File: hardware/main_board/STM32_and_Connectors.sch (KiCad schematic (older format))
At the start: 26 parts, among them J401 Conn_01x20, J402 Conn_01x20, J403 Conn_01x04, J404 Conn_01x04, J405 Conn_01x04, J406 MOTOR 1, J407 MOTOR 2, J408 POWER, J409 SKITTLE PICKUP, J410 LIMIT SWITCHES, J411 SERVO, Q401 SSM3K333R

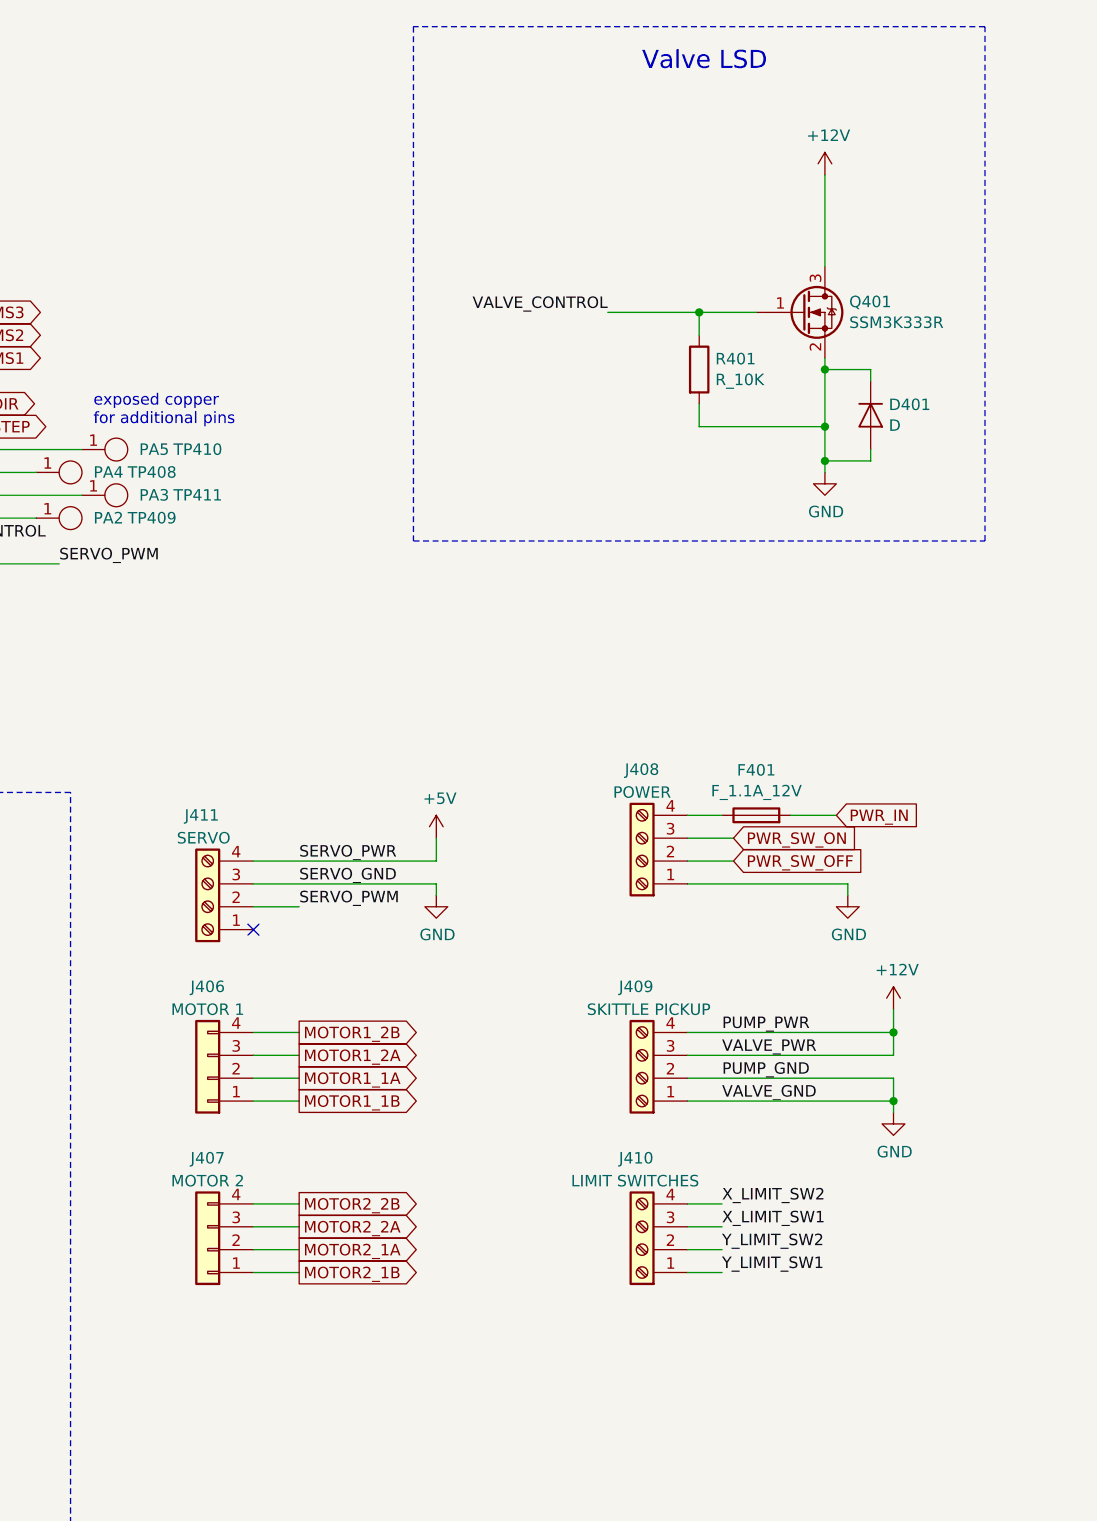
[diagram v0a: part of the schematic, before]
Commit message: fixed valve lsd circuit
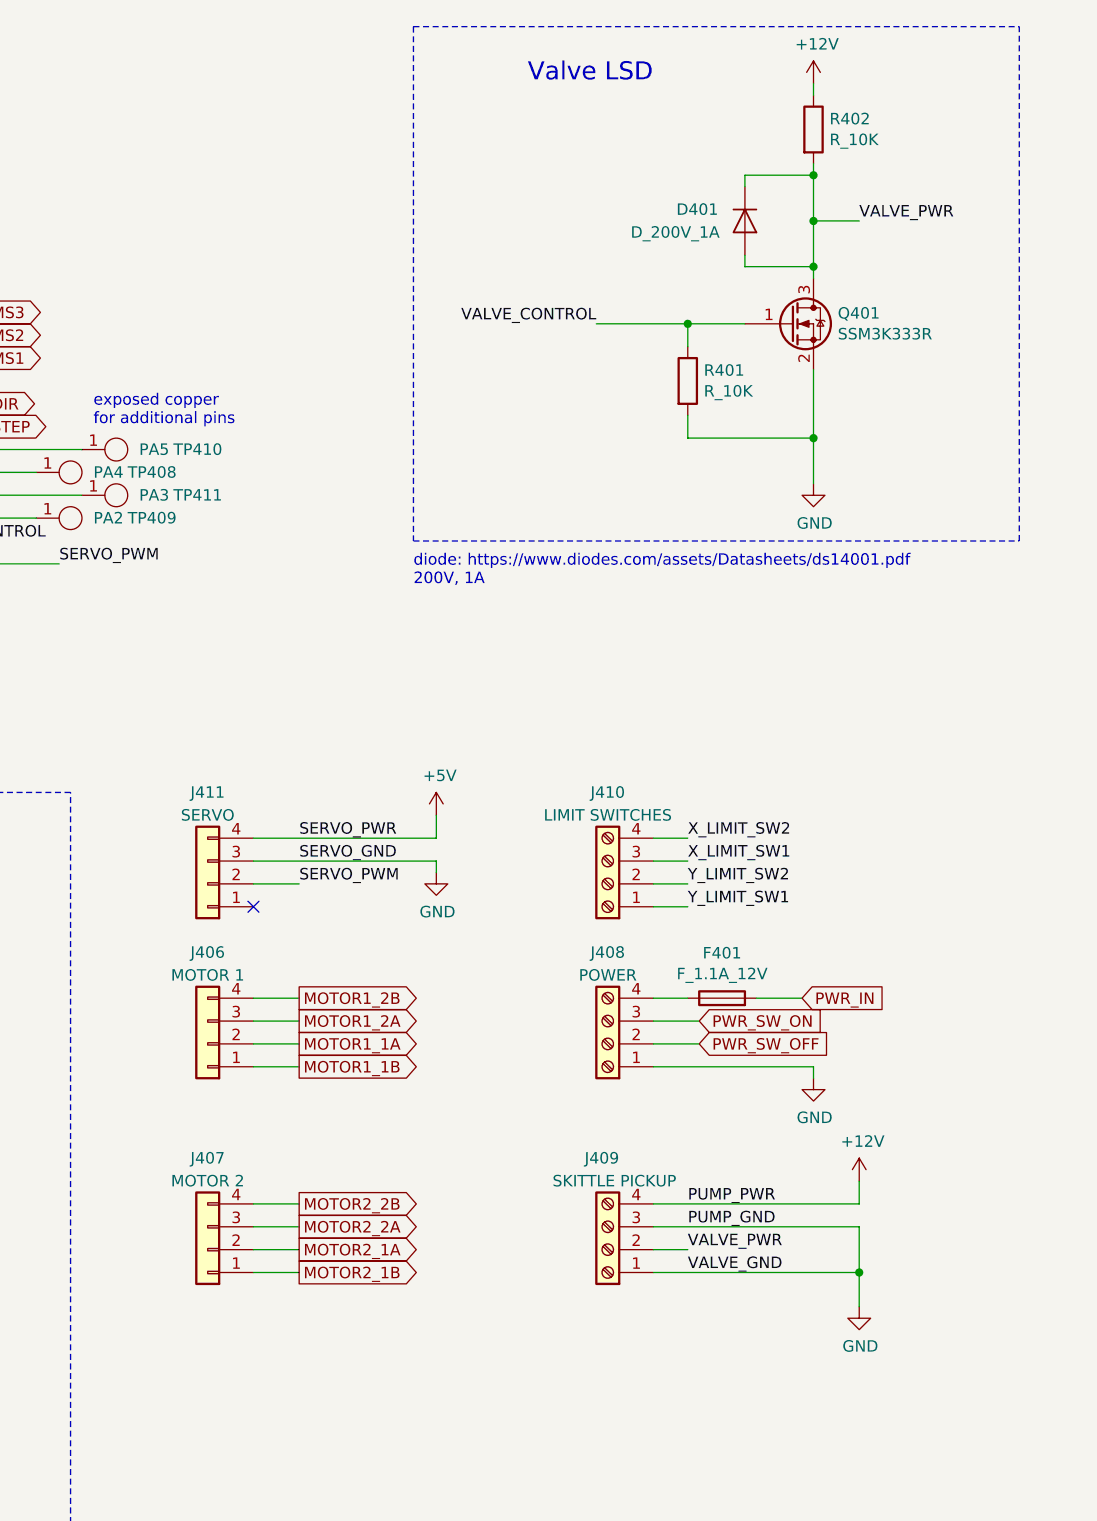
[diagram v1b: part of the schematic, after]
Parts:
- removed J411: SERVO, symbol Connector:Screw_Terminal_01x04
- added J411: SERVO, symbol Connector_Generic:Conn_01x04
- added R402: R_10K, footprints:R_0805_OEM, symbol formula:R_10K
- D401: value D -> D_200V_1A
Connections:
- net +12V: now also R402.1; no longer J409.3 (Pin_3), Q401.3 (D)
- net +5V: now also J411.4 (Pin_4)
- net GND: now also J409.3 (Pin_3), J411.3 (Pin_3); no longer D401.1 (K), D401.2 (A), J409.2 (Pin_2)
- net PA0(PWM): now also J411.2 (Pin_2)
- new net VALVE_PWR: D401.1 (K), D401.2 (A), J409.2 (Pin_2), Q401.3 (D), R402.2
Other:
- note added: "diode: https://www.diodes.com/assets/Datasheets/ds14001.pdf\n200V, 1A"
- moved on the sheet: F401, J406, J408, J409, Q401, R401

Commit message: added connector for powering limit switches
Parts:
- added J412: LIMIT SWITCHES POWER, symbol Connector_Generic:Conn_01x08
- added R403, R404, R405, R406: R_10K, footprints:R_0805_OEM, symbol formula:R_10K
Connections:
- net +3V3: now also R403.1, R404.1, R405.1, R406.1
- net GND: now also J412.1 (Pin_1), J412.3 (Pin_3), J412.5 (Pin_5), J412.7 (Pin_7)
- new net X_LIMIT_SW1_PWR: J412.6 (Pin_6), R404.2
- new net X_LIMIT_SW2_PWR: J412.8 (Pin_8), R403.2
- new net Y_LIMIT_SW1_PWR: J412.2 (Pin_2), R406.2
- new net Y_LIMIT_SW2_PWR: J412.4 (Pin_4), R405.2
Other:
- moved on the sheet: F401, J403, J404, J405, J406, J407, J408, J409, J410, J411

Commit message: Added skittle_pnp symbol and footprint library
Added 10uF tantalum capacitor and diode to the
skittle_pnp symbol and footprints libraries.
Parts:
- removed D401: D_200V_1A, symbol Device:D
- removed J410: LIMIT SWITCHES, symbol Connector:Screw_Terminal_01x04
- removed Q401: SSM3K333R, footprints:SOT-23F, symbol formula:SSM3K333R
- removed R401, R402: R_10K, footprints:R_0805_OEM, symbol formula:R_10K
- J412: value LIMIT SWITCHES POWER -> LIMIT SWITCHES
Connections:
- net X_LIMIT_SW1_PWR is gone; now on net PB9: J412.6 (Pin_6), R404.2
- net X_LIMIT_SW2_PWR is gone; now on net PB8: J412.8 (Pin_8), R403.2
- net Y_LIMIT_SW1_PWR is gone; now on net (SCK)PB13: J412.2 (Pin_2), R406.2
- net Y_LIMIT_SW2_PWR is gone; now on net (SS)PB12: J412.4 (Pin_4), R405.2
- net GND: now also J409.2 (Pin_2); no longer J409.1 (Pin_1)
- net VALVE_PWR: now also J409.1 (Pin_1); no longer J409.2 (Pin_2)
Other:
- note added: "MIN --> (0,0)"
- note added: "PWR wired to the NC pin \nGND wired to the G pin"
- note added: "STM32 has an internal 5V - 3.3V Regulator \nwhich will be used to supply 3.3V for the rest \nof the components"
- note removed: "Valve LSD"
- note removed: "diode: https://www.diodes.com/assets/Datasheets/ds14001.pdf\n200V, 1A"
- moved on the sheet: F401, J403, J404, J405, J406, J407, J408, J409, J411, J412, R403, R404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

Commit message: final schematic and layout
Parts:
- removed J411: SERVO, symbol Connector_Generic:Conn_01x04
- added J410: MOTOR 2, skittle_pnp:SULLINS_PPTC041LFBN-RC, symbol Connector_Generic:Conn_01x04
- F401: footprint Fuse_Holders_and_Fuses:Fuse_SMD1206_Reflow -> skittle_pnp:1206L075SLYR
- J401, J402: footprint (none) -> skittle_pnp:RHDR20W80P0X254_1X20_5130X254X880P
- J403: value Conn_01x04 -> I2C; footprint (none) -> skittle_pnp:SULLINS_PPTC041LFBN-RC
- J404: value Conn_01x04 -> USART 1; footprint (none) -> skittle_pnp:SULLINS_PPTC041LFBN-RC
- J405: value Conn_01x04 -> USART 2; footprint (none) -> skittle_pnp:SULLINS_PPTC041LFBN-RC
- J406: value MOTOR 1 -> SERVO; footprint (none) -> skittle_pnp:SULLINS_PPTC041LFBN-RC
- J407: value MOTOR 2 -> MOTOR 1; footprint (none) -> skittle_pnp:SULLINS_PPTC041LFBN-RC
- J408, J409: footprint (none) -> skittle_pnp:CUI_TB006-508-04BE
- J412: footprint (none) -> skittle_pnp:RHDR8W80P0X254_1X8_2082X254X850P
- TP403: value PA8 -> PA0
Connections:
- net (SCK)PB13: now also J412.4 (Pin_4), R405.2; no longer J412.2 (Pin_2), R406.2
- net (SS)PB12: now also J412.2 (Pin_2), R406.2; no longer J412.4 (Pin_4), R405.2
- net +5V: now also J406.4 (Pin_4)
- net GND: now also J406.3 (Pin_3); no longer J409.2 (Pin_2)
- net MOTOR1_1A: now also J407.2 (Pin_2); no longer J406.2 (Pin_2)
- net MOTOR1_1B: now also J407.1 (Pin_1); no longer J406.1 (Pin_1)
- net MOTOR1_2A: now also J407.3 (Pin_3); no longer J406.3 (Pin_3)
- net MOTOR1_2B: now also J407.4 (Pin_4); no longer J406.4 (Pin_4)
- net MOTOR1_DIR: now also J401.13 (Pin_13); no longer J401.9 (Pin_9)
- net MOTOR1_MS1: now also J401.9 (Pin_9); no longer J401.11 (Pin_11)
- net MOTOR1_MS2: now also J401.10 (Pin_10); no longer J401.12 (Pin_12)
- net MOTOR1_MS3: now also J401.11 (Pin_11); no longer J401.13 (Pin_13)
- net MOTOR1_STEP: now also J401.12 (Pin_12); no longer J401.8 (Pin_8)
- net MOTOR1_~EN: now also J401.8 (Pin_8); no longer J401.10 (Pin_10)
- net MOTOR2_1A: now also J410.2 (Pin_2); no longer J407.2 (Pin_2)
- net MOTOR2_1B: now also J410.1 (Pin_1); no longer J407.1 (Pin_1)
- net MOTOR2_2A: now also J410.3 (Pin_3); no longer J407.3 (Pin_3)
- net MOTOR2_2B: now also J410.4 (Pin_4); no longer J407.4 (Pin_4)
- net MOTOR2_DIR: now also J402.11 (Pin_11); no longer J402.12 (Pin_12)
- net MOTOR2_MS1: now also J402.15 (Pin_15); no longer J402.14 (Pin_14)
- net MOTOR2_MS2: now also J402.14 (Pin_14); no longer J402.15 (Pin_15)
- net MOTOR2_MS3: now also J402.13 (Pin_13); no longer J402.16 (Pin_16)
- net MOTOR2_STEP: now also J402.12 (Pin_12); no longer J402.11 (Pin_11)
- net MOTOR2_~EN: now also J402.16 (Pin_16); no longer J402.13 (Pin_13)
- net PA0(PWM): now also TP403.1
- net PA8: now also J406.2 (Pin_2); no longer TP403.1
- net PB8: now also J412.6 (Pin_6), R404.2; no longer J412.8 (Pin_8), R403.2
- net PB9: now also J412.8 (Pin_8), R403.2; no longer J412.6 (Pin_6), R404.2
- net PA1 renamed VALVE_CONTROL
- new net VALVE_GND: J409.2 (Pin_2)
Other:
- note added: "Motor 1"
- note added: "Motor 2\n"
- note added: "PWR wired to the NO pin \nGND wired to the G pin"
- note added: "Power"
- note added: "Servo"
- note added: "Valve and Pump"
- note added: "add pullup for i2c"
- note removed: "PWR wired to the NC pin \nGND wired to the G pin"
- note removed: "STM32 has an internal 5V - 3.3V Regulator \nwhich will be used to supply 3.3V for the rest \nof the components"
- moved on the sheet: TP403

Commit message: added final schematic and layout
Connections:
- net +5V: no longer J401.18 (Pin_18)
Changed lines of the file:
@@
-	1    0    0    -1
-$EndComp
-$Comp
-L power:+5V #PWR0402
-U 1 1 619589F2
-P 3100 1300
-F 0 "#PWR0402" H 3100 1150 50  0001 C CNN
-F 1 "+5V" V 3100 1500 50  0000 C CNN
-F 2 "" H 3100 1300 50  0001 C CNN
-F 3 "" H 3100 1300 50  0001 C CNN
-	1    3100 1300
 	1    0    0    -1
 $EndComp
@@
 	3000 3400 3250 3400
 Wire Wire Line
-	3100 1300 3100 3200
-Wire Wire Line
-	3100 3200 3250 3200
-Wire Wire Line
 	3250 3300 3150 3300
